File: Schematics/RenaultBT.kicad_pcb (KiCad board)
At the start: 2 copper layers, 160 x 100.3 mm, 57 parts, among them J1 PowerSupply, J2 SPDIF_Output, J3 HU_CDC_Interface, Q1 2N7000, Q2 2N7000, Q3 2N7000, Q4 2N7000, U1 LM2575-5.0BT, U2 LM1117-3.3, U3 WM8804, U4 CSRA64215, U5 74HC04, U6 STM32F103, Y1 12Mhz

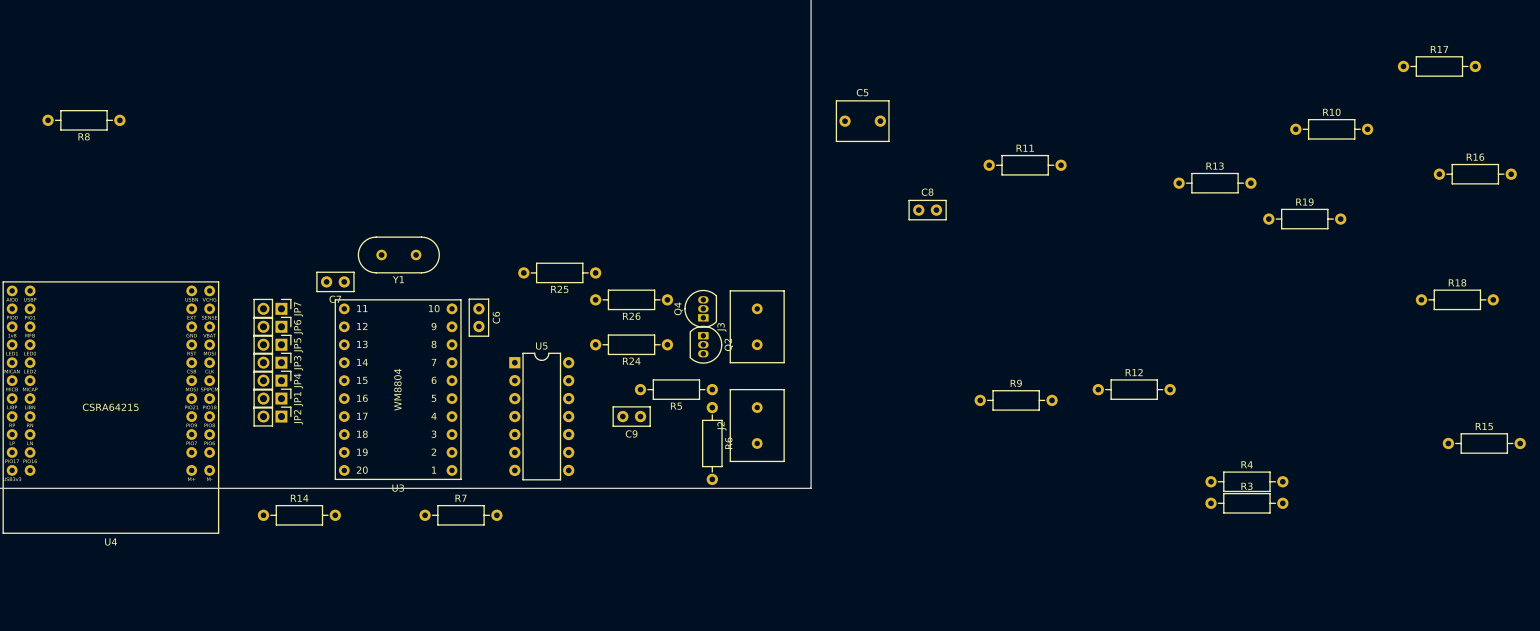
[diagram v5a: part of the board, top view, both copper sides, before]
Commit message: Fixed library settings; modified PCB design
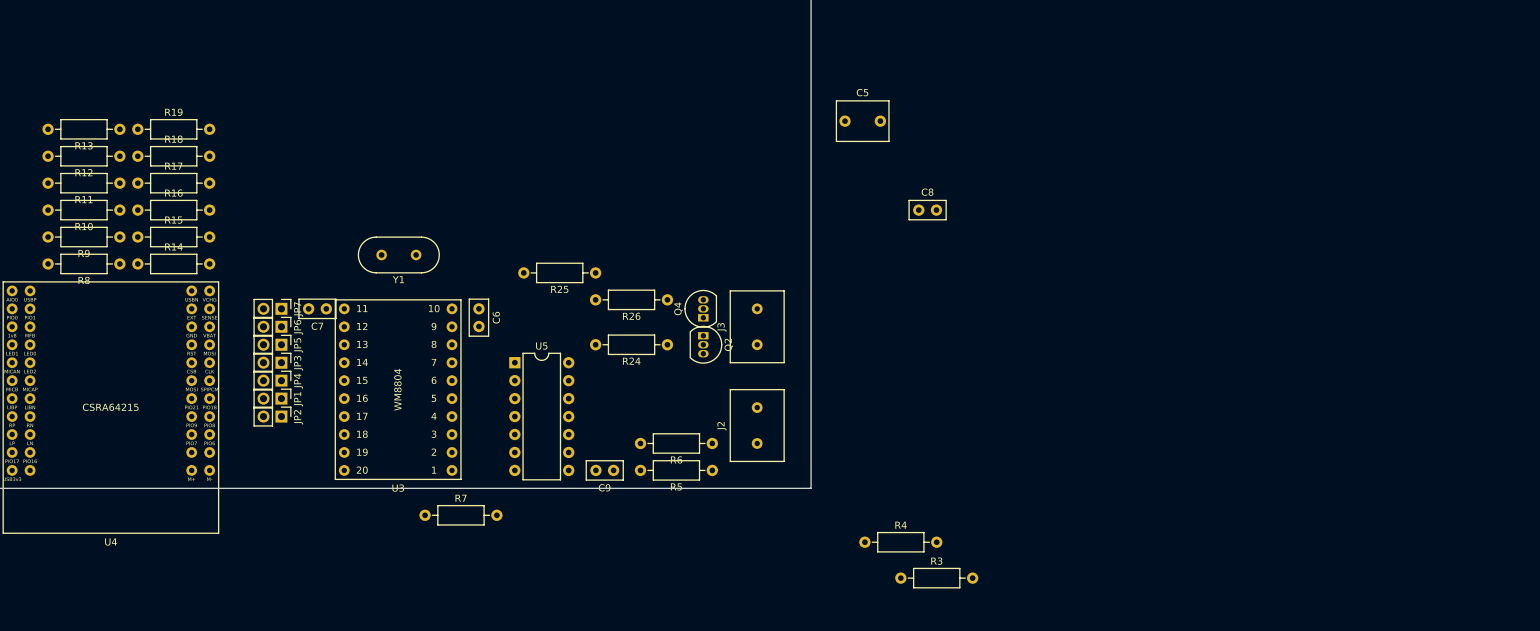
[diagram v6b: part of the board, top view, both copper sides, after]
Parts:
- moved R15 187.7 mm to (115.6, 102.9)
- moved R16 184.2 mm to (115.6, 99.1)
- moved R18 182.7 mm to (115.6, 91.4)
- moved R17 179.8 mm to (115.6, 95.2)
- moved R10 166.8 mm to (113.0, 99.1), turned to 180 degrees
- moved R19 160.5 mm to (115.6, 87.6)
- moved R13 150.1 mm to (113.0, 87.6), turned to 180 degrees
- moved R12 142.3 mm to (113.0, 91.4), turned to 180 degrees
- moved R9 123.9 mm to (113.0, 102.9), turned to 180 degrees
- moved R11 123.0 mm to (113.0, 95.2), turned to 180 degrees
- moved R4 49.7 mm to (218.4, 146.1)
- moved R3 45.1 mm to (223.5, 151.1)
- moved R14 39.8 mm to (115.6, 106.7)
- moved R8 20.3 mm to (113.0, 106.7)
- moved R5 11.4 mm to (196.8, 135.9)
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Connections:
- J2 pad 1: /I2SToSPDIF/DGND -> /I2SToSPDIF/SPDIF_OUTPUT
- J2 pad 2: /I2SToSPDIF/SPDIF_OUTPUT -> /I2SToSPDIF/DGND

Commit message: Updated PCB design
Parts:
- moved R4 52.6 mm to (166.4, 153.7), turned to 90 degrees
- moved R3 49.6 mm to (174.0, 153.7), turned to 90 degrees
- moved R7 21.6 mm to (142.2, 125.7), turned to 90 degrees
- moved C6 5.39 mm to (160.0, 109.2), turned to 0 degrees
- moved C7 4.58 mm to (144.8, 109.2)
- moved Y1 2.54 mm to (154.9, 108.0)
- moved C9 2.50 mm to (185.4, 135.9)
- moved R5 1.27 mm to (198.1, 135.9)
- moved R6 1.27 mm to (198.1, 132.1)

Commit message: Updated PCB design
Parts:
- R3: footprint Resistor_THT:R_Axial_DIN0207_L6.3mm_D2.5mm_P10.16mm_Horizontal -> Resistor_THT:R_Axial_DIN0204_L3.6mm_D1.6mm_P5.08mm_Vertical
- R4: footprint Resistor_THT:R_Axial_DIN0207_L6.3mm_D2.5mm_P10.16mm_Horizontal -> Resistor_THT:R_Axial_DIN0204_L3.6mm_D1.6mm_P2.54mm_Vertical
- R6: footprint Resistor_THT:R_Axial_DIN0207_L6.3mm_D2.5mm_P10.16mm_Horizontal -> Resistor_THT:R_Axial_DIN0207_L6.3mm_D2.5mm_P5.08mm_Vertical
- moved C8 81.7 mm to (146.1, 115.6), turned to 90 degrees
- moved Q3 55.2 mm to (171.4, 133.3), turned to 90 degrees
- moved C5 49.8 mm to (175.3, 115.6), turned to 180 degrees
- moved R4 30.6 mm to (168.9, 123.2)
- moved R3 28.1 mm to (171.4, 125.7)
- moved R26 19.1 mm to (190.5, 92.7)
- moved J3 19.0 mm to (203.2, 96.5)
- moved Q2 19.0 mm to (195.6, 97.8)
- moved Q4 19.0 mm to (195.6, 95.2)
- moved R24 19.0 mm to (190.5, 99.1)
- moved R25 19.0 mm to (180.3, 88.9)
- moved U5 12.6 mm to (177.8, 129.5), turned to 90 degrees
- moved C6 6.35 mm to (166.4, 109.2)
- moved C7 6.35 mm to (151.1, 109.2)
- moved R7 6.35 mm to (148.6, 125.7)
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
